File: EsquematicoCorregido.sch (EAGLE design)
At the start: 24 parts, among them IC1 OPA991TIDCKR, IC2 AD8226ARZ-RL, IC3 OPA991TIDCKR, IC4 ESP32-S3-WROOM-1-N16R8, IC5 OPA991TIDCKR, IC6 MAX30102EFD+T, IC7 LP38692MP-3.3_NOPB, IC8 LP38692MP-1.8_NOPB, IC9 REF2033AIDDCT

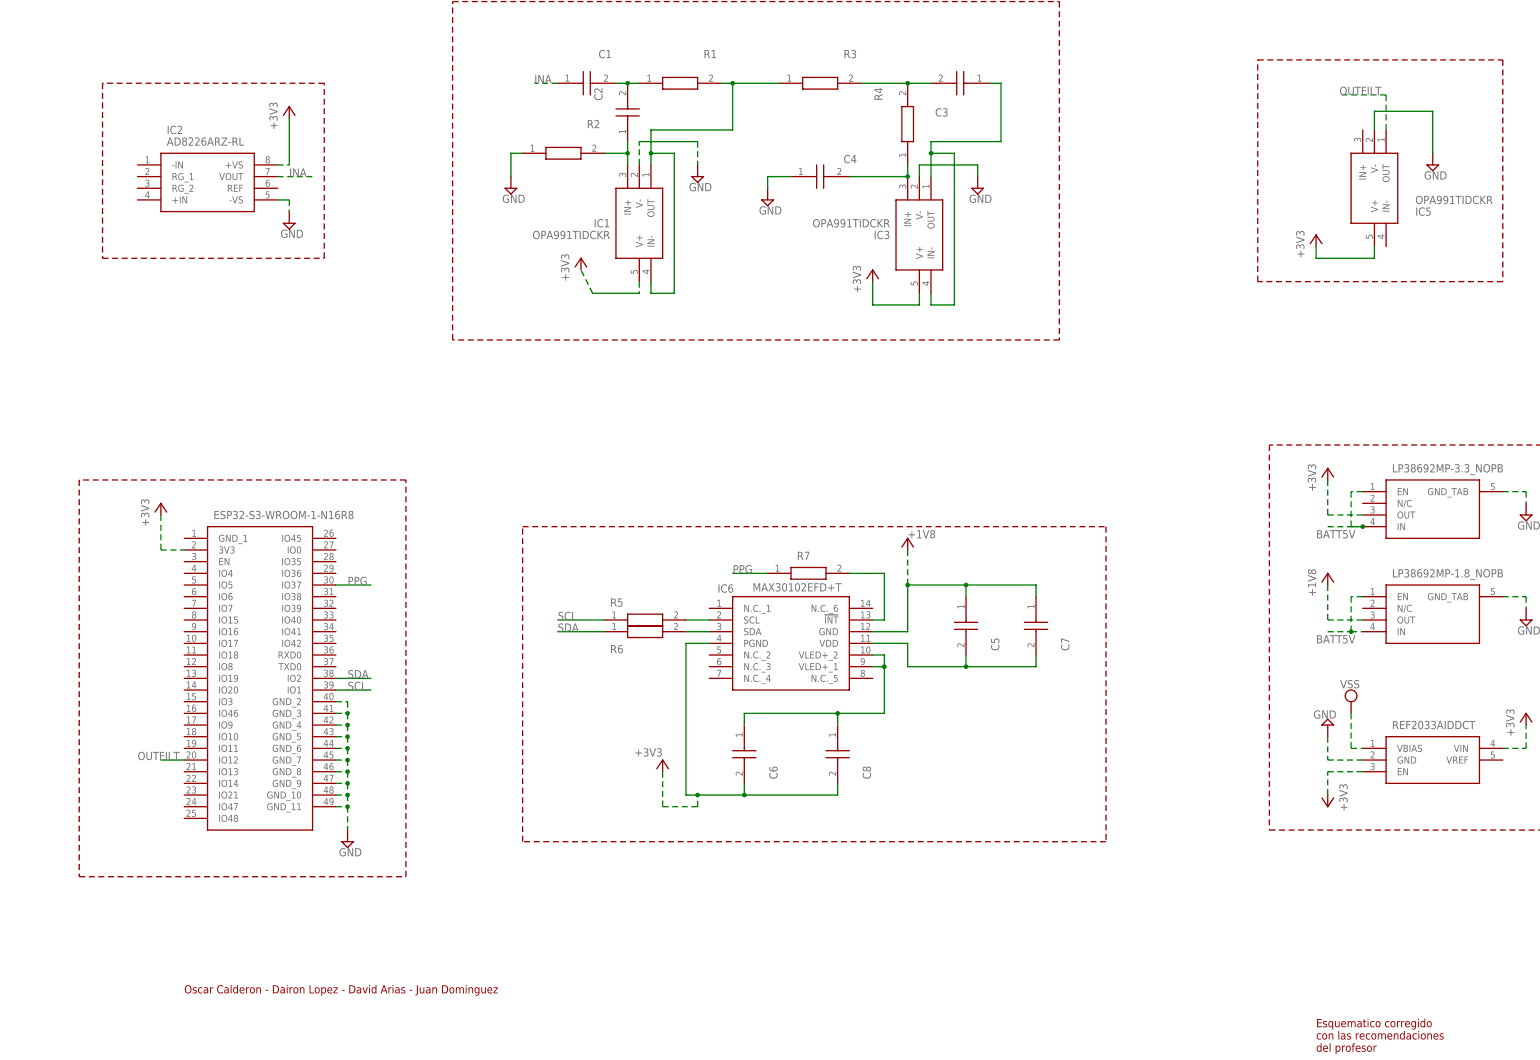
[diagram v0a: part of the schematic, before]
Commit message: Se corrigieron algunos bloques y se anoto lo faltante
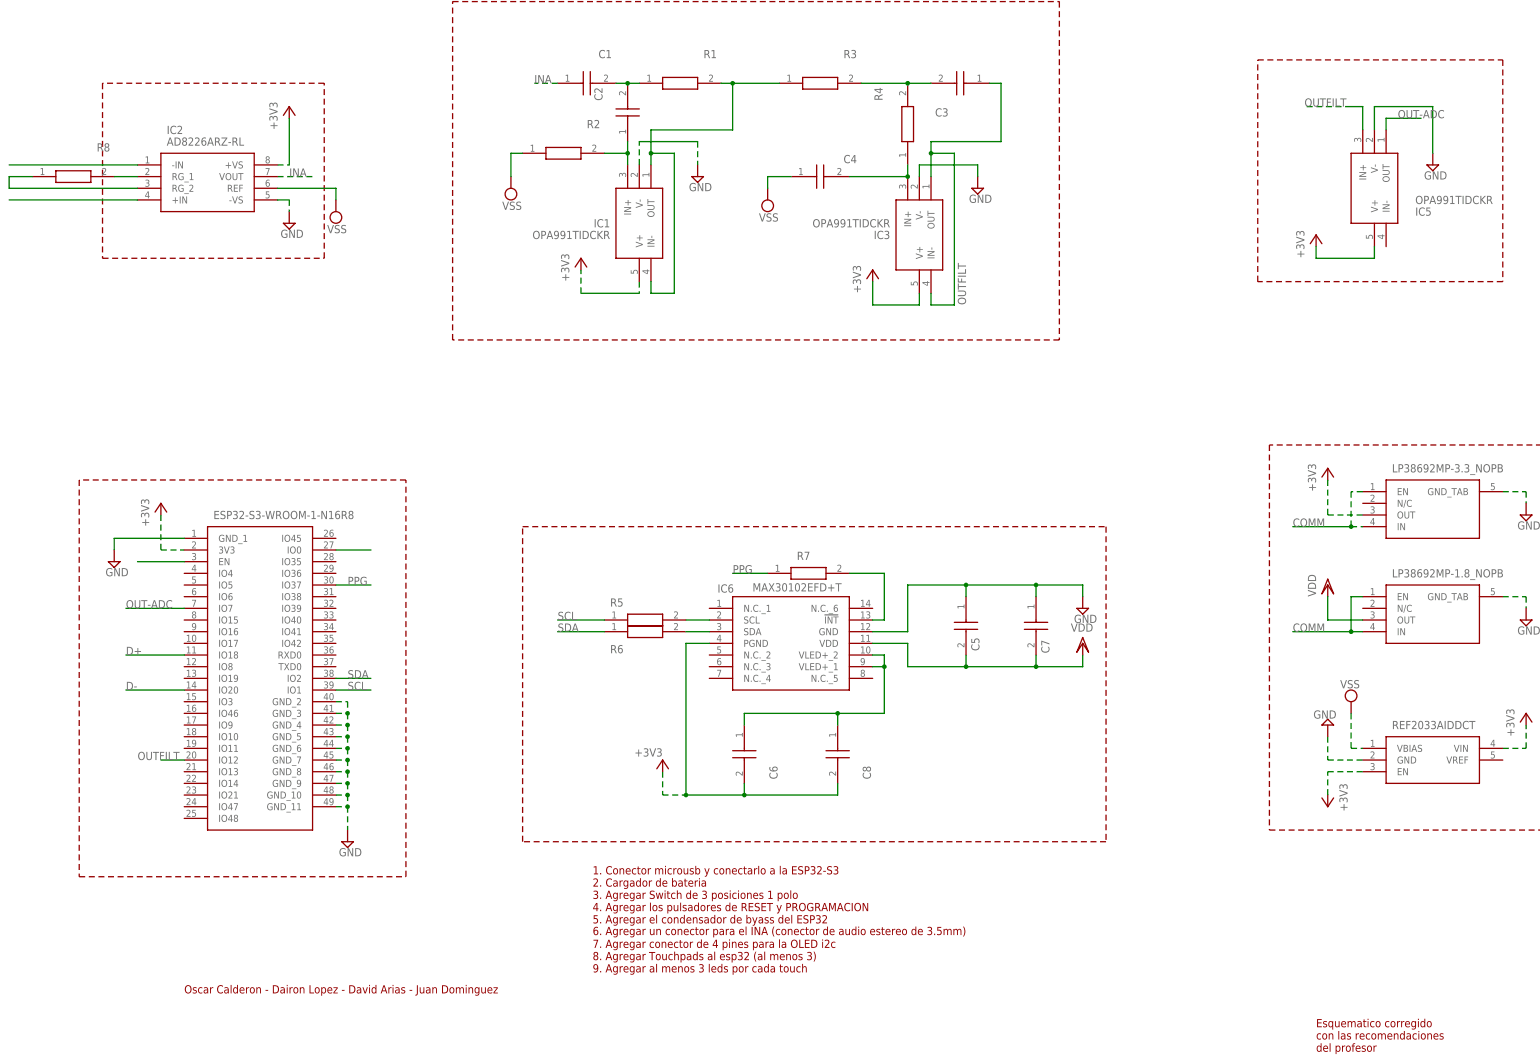
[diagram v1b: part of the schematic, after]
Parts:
- added R8: RN73H1JTTD1043B50, RN73H1JTTD1043B50:RN73H1JTTD1043B50
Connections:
- removed net +1V8: C5.1, C7.1, IC6.GND, IC8.EN, IC8.IN
- removed net BATT5V: IC7.EN, IC7.IN
- removed net N$20: C3.1, IC3.IN-, IC3.OUT
- new net COMM: IC7.EN, IC7.IN, IC8.EN, IC8.IN
- new net D+: IC4.IO18
- new net D-: IC4.IO20
- new net N$10: IC4.EN
- new net N$11: IC2.RG_2, R8.1
- new net N$14: IC2.-IN
- new net N$15: IC2.+IN
- new net N$5: IC4.IO0
- new net OUT-ADC: IC4.IO7, IC5.OUT
- new net VDD: C5.2, C7.2, IC6.VDD, IC8.OUT
- net +3V3: no longer IC8.OUT
- net GND: now also C5.1, C7.1, IC4.GND_1, IC6.GND; no longer C4.1, R2.1
- net N$7: now also IC2.RG_1, R8.2; no longer C5.2, C7.2, IC6.VDD
- net OUTFILT: now also C3.1, IC3.IN-, IC3.OUT, IC5.IN+; no longer IC5.OUT
- net VSS: now also C4.1, IC2.REF, R2.1
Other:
- note added: "1. Conector microusb y conectarlo a la ESP32-S3 2. Cargador de bateria 3. Agregar Switch de 3 posiciones 1 polo 4. Agregar los pulsadores de RESET y PROGRAMACION 5. Agregar el condensador de byass del ESP32"
- note added: "6. Agregar un conector para el INA (conector de audio estereo de 3.5mm)"
- note added: "7. Agregar conector de 4 pines para la OLED i2c 8. Agregar Touchpads al esp32 (al menos 3) 9. Agregar al menos 3 leds por cada touch"

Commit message: ultima actualización, correcion de los puntos
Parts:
- added BAT1: (no value), special:BATTERY
- added C10, C11, C9: GRM155C80G106ME18D, GRM155C80G106ME18D:GRM155C80G106ME18D
- added D1: HLMP6, display-hp:HLMP6
- added IC10: MCP73831T-2ACI_OT, MCP73831T-2ACI_OT:MCP73831T-2ACI_OT
- added J1, J2: USB3131-30-0230-A_REVB, USB3131-30-0230-A_REVB:USB3131-30-0230-A_REVB
- added R10, R11: (no value), resistor-shunt:BVS
- added R2K: ERJ-UP6D2001V, ERJ-UP6D2001V:ERJ-UP6D2001V
- added R9: CRCW0805220RFKTAHP, CRCW0805220RFKTAHP:CRCW0805220RFKTAHP
- added S1, S2: BUTT-2, BUTT-2:BUTT-2
- added U1: DM-OLED096-636, DM-OLED096-636:DM-OLED096-636
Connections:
- removed net N$5: IC4.IO0
- new net 3V3: C11.1, R10.1, R11.1
- new net 5V: C9.2, D1.A, IC10.VDD, J2.VCC
- new net EN: R10.2, S1.1
- new net IO0: IC4.IO0, R11.2, S2.1
- new net N$16: D1.K, R9.2
- new net N$17: IC10.PROG, R2K.2
- new net N$18: IC10.STAT, R9.1
- new net SCL_DSP: IC4.IO9, U1.SCL
- new net SDA_DSP: IC4.IO8, U1.SDA
- net +3V3: now also J1.VCC, U1.VCC_IN
- net D+: now also IC4.IO20, J1.D+; no longer IC4.IO18
- net D-: now also IC4.IO19, J1.D-; no longer IC4.IO20
- net GND: now also C10.1, C11.2, C9.1, IC10.VSS, J1.GND, J1.SHIELD, J2.GND, J2.SHIELD, R2K.1, S1.2, S2.2, U1.GND
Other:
- note added: "1. Conector microusb y conectarlo a la ESP32-S3 (ya) 2. Cargador de bateria(ya) 3. Agregar Switch de 3 posiciones 1 polo 4. Agregar los pulsadores de RESET y PROGRAMACION (ya) 5. Agregar el condensador de byass del ESP32 (ya)"
- note added: "7. Agregar conector de 4 pines para la OLED i2c (ya) 8. Agregar Touchpads al esp32 (al menos 3) 9. Agregar al menos 3 leds por cada touch"
- note removed: "1. Conector microusb y conectarlo a la ESP32-S3 2. Cargador de bateria 3. Agregar Switch de 3 posiciones 1 polo 4. Agregar los pulsadores de RESET y PROGRAMACION 5. Agregar el condensador de byass del ESP32"
- note removed: "7. Agregar conector de 4 pines para la OLED i2c 8. Agregar Touchpads al esp32 (al menos 3) 9. Agregar al menos 3 leds por cada touch"
- moved on the sheet: C1, C2, C3, C4, C5, C6, C7, C8, IC1, IC2, IC3, IC5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

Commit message: Se corrigio el esquematico y packages
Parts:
- removed BAT1: (no value), special:BATTERY
- removed R10, R11: (no value), resistor-shunt:BVS
- removed S1, S2: BUTT-2, BUTT-2:BUTT-2
- added BATT: 1769, 1769:1769
- added C12: (no value), rcl:C-EUC0805
- added POWER: PCM13SMTR, PCM13SMTR:PCM13SMTR
- added R12, R13: (no value), rcl:R-EU_R0805
- added S3, S4: PTS526SK15SMTR2_LFS, PTS526SK15SMTR2_LFS:PTS526SK15SMTR2_LFS
- C1, C3: value QXK2E475KTP -> (none); device QXK2E475KTP:QXK2E475KTP -> rcl:C-EUC0805
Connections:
- new net +5V: C9.2, D1.A, IC10.VDD, POWER.1
- new net BATT+: BATT.2, C10.2, IC10.VBAT, POWER.2
- net 3V3: now also R12.2, R13.2; no longer R10.1, R11.1
- net 5V: no longer C9.2, D1.A, IC10.VDD
- net COMM: now also POWER.3
- net EN: now also R13.1; no longer R10.2, S1.1
- net GND: now also BATT.1, BATT.3, BATT.4; no longer S1.2, S2.2
- net IO0: now also R12.1; no longer R11.2, S2.1

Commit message: ultimas actualizaciones
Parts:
- removed C7: C0805J104K1RACAUTO, C0805J104K1RACAUTO:C0805J104K1RACAUTO
- removed U1: DM-OLED096-636, DM-OLED096-636:DM-OLED096-636
- added SV1: (no value), con-lstb:MA04-1
- C2, C5, C6: value QXK2E475KTP -> (none); device QXK2E475KTP:QXK2E475KTP -> rcl:C-EUC0805
- C4: value C2220X205K1RLCAUTO -> (none); device C2220X205K1RLCAUTO:C2220X205K1RLCAUTO -> rcl:C-EUC0805
- C8: value C0805J104K1RACAUTO -> (none); device C0805J104K1RACAUTO:C0805J104K1RACAUTO -> rcl:C-EUC0805
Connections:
- new net N$21: SV1.1
- net +3V3: now also C4.1, C6.1, SV1.2; no longer C6.2, C8.2, U1.VCC_IN
- net EN: now also S3.NO_1
- net GND: now also C5.2, C8.2, S3.COM_1, S4.COM_1; no longer C5.1, C7.1, U1.GND
- net IO0: now also S4.NO_1
- net N$2: now also C12.2; no longer C2.2
- net N$3: now also C12.1; no longer C2.1
- net N$4: now also C2.2; no longer C4.2
- net N$9: now also C4.2, C6.2; no longer C6.1, C8.1
- net SCL_DSP: now also SV1.4; no longer U1.SCL
- net SDA_DSP: now also SV1.3; no longer U1.SDA
- net VDD: now also C5.1, C8.1; no longer C5.2, C7.2
- net VSS: now also C2.1; no longer C4.1
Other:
- note added: "1. Conector microusb y conectarlo a la ESP32-S3 (ya) 2. Cargador de bateria(ya) 3. Agregar Switch de 3 posiciones 1 polo (ya) 4. Agregar los pulsadores de RESET y PROGRAMACION (ya) 5. Agregar el condensador de byass del ESP32 (ya)"
- note removed: "1. Conector microusb y conectarlo a la ESP32-S3 (ya) 2. Cargador de bateria(ya) 3. Agregar Switch de 3 posiciones 1 polo 4. Agregar los pulsadores de RESET y PROGRAMACION (ya) 5. Agregar el condensador de byass del ESP32 (ya)"
- moved on the sheet: C11, C12, POWER, R12, R13, S3, S4

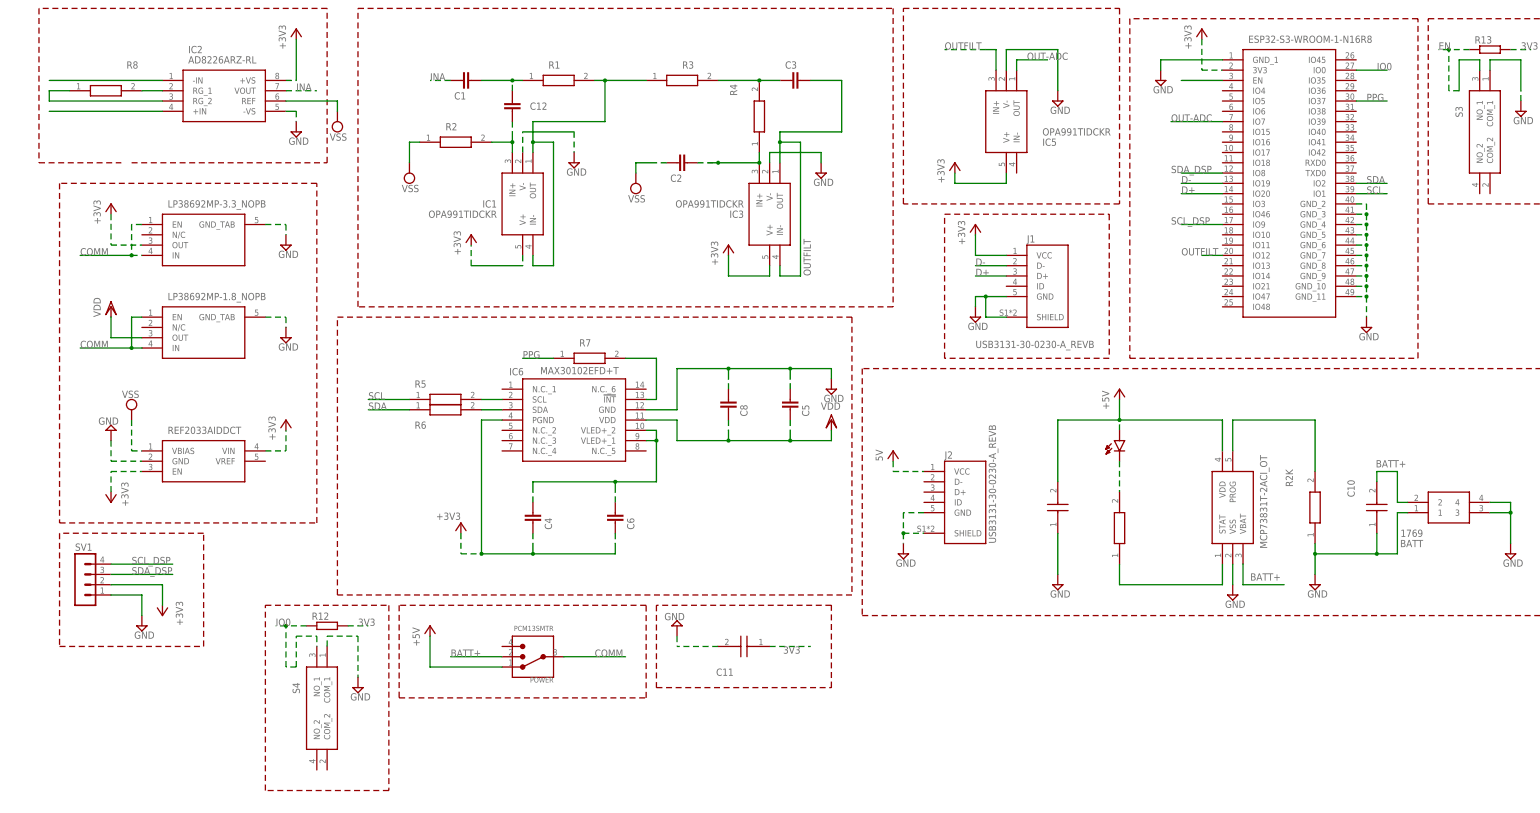
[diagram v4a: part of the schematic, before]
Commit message: fix: PCB and schematic errors fixed
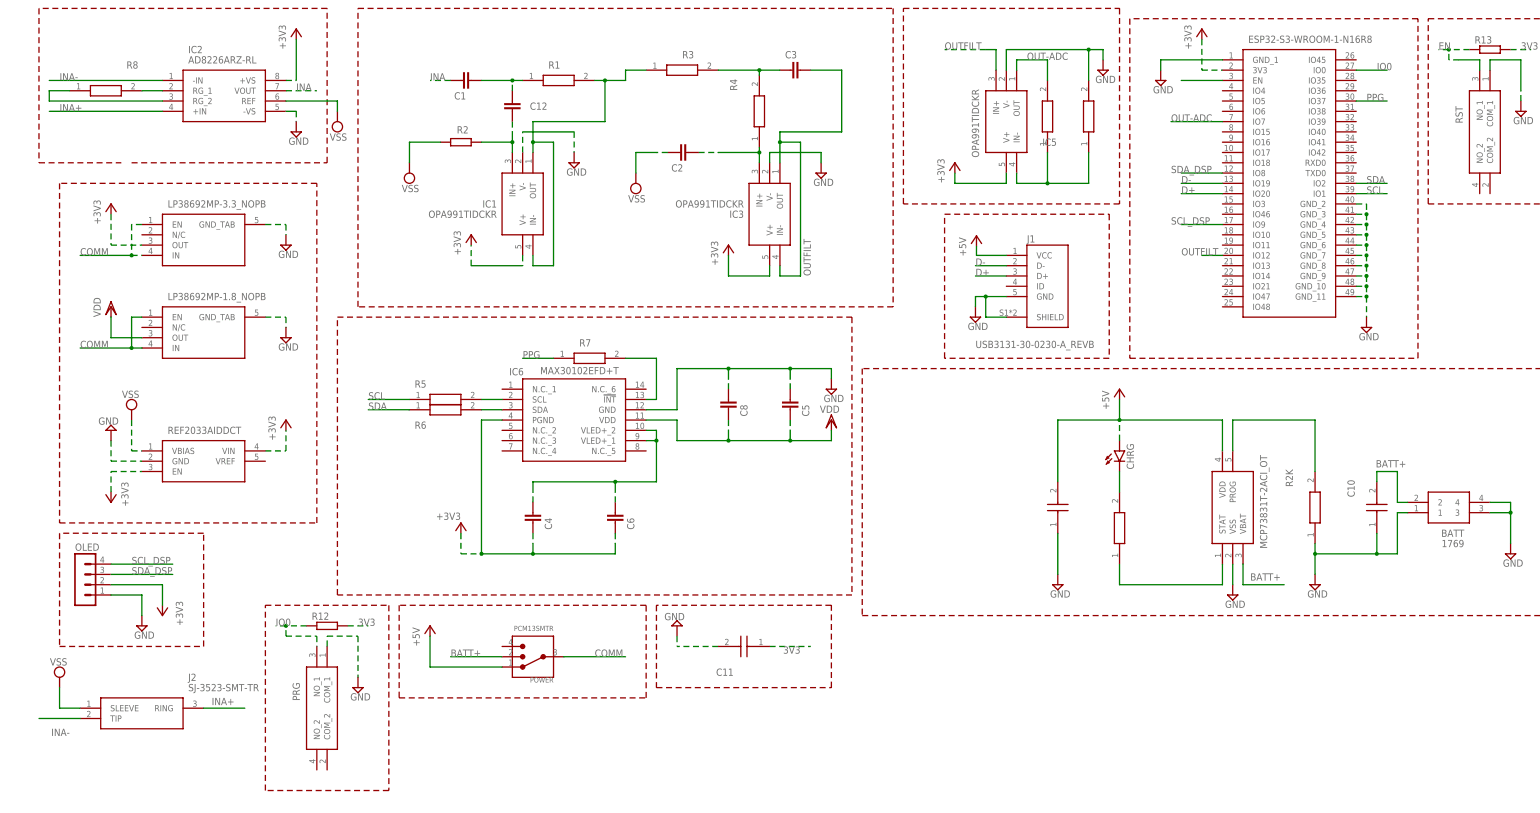
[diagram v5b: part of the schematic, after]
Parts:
- removed D1: HLMP6, display-hp:HLMP6
- added CHRG: (no value), led:LEDCHIP-LED0805
- added R10, R11: CRCW0805220RFKTAHP, CRCW0805220RFKTAHP:CRCW0805220RFKTAHP
- J2: value USB3131-30-0230-A_REVB -> SJ-3523-SMT-TR; device USB3131-30-0230-A_REVB:USB3131-30-0230-A_REVB -> SJ-3523-SMT-TR:SJ-3523-SMT-TR
- R2: value RN73H1JTTD1043B50 -> (none); device RN73H1JTTD1043B50:RN73H1JTTD1043B50 -> rcl:R-EU_R0805
- renumbered S3 to RST, S4 to PRG, SV1 to OLED
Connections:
- removed net 5V: J2.VCC
- removed net N$15: IC2.+IN
- removed net N$16: D1.K, R9.2
- new net INA+: IC2.+IN, J2.RING
- new net INA-: IC2.-IN, J2.TIP
- new net N$5: IC5.IN-, R10.1, R11.1
- net +3V3: no longer J1.VCC
- net +5V: now also CHRG.A, J1.VCC; no longer D1.A
- net GND: now also R11.2; no longer J2.GND, J2.SHIELD
- net N$14: now also CHRG.C, R9.2; no longer IC2.-IN
- net OUT-ADC: now also R10.2
- net VSS: now also J2.SLEEVE
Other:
- moved on the sheet: C2, C3, R3, R4

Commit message: Avance PCB
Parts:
- removed J1: USB3131-30-0230-A_REVB, USB3131-30-0230-A_REVB:USB3131-30-0230-A_REVB
- removed R2K: ERJ-UP6D2001V, ERJ-UP6D2001V:ERJ-UP6D2001V
- added J3: USB4216-03-A, USB4216-03-A:USB4216-03-A
- added R14, R15, R16: (no value), rcl:R-EU_R0805
- C10, C11, C9: value GRM155C80G106ME18D -> (none); device GRM155C80G106ME18D:GRM155C80G106ME18D -> rcl:C-EUC0805
- R1: value RN73H1ETTP4812D25 -> (none); device RN73H1ETTP4812D25:RN73H1ETTP4812D25 -> rcl:R-EU_R0805
- R9: value CRCW0805220RFKTAHP -> (none); device CRCW0805220RFKTAHP:CRCW0805220RFKTAHP -> rcl:R-EU_R0805
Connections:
- removed net N$10: IC4.EN
- new net N$16: J3.CC1, R15.1
- new net N$19: J3.CC2, R16.2
- net +3V3: now also R12.2, R13.2
- net +5V: now also C9.1, J3.VBUS_1, J3.VBUS_2; no longer C9.2, J1.VCC
- net 3V3: now also C11.2; no longer C11.1, R12.2, R13.2
- net BATT+: now also C10.1; no longer C10.2
- net D+: now also J3.DP1, J3.DP2; no longer J1.D+
- net D-: now also J3.DN1, J3.DN2; no longer J1.D-
- net EN: now also IC4.EN
- net GND: now also C10.2, C11.1, C9.2, J3.GND_1, J3.GND_2, J3.GND_3, J3.GND_4, J3.GND_5, J3.GND_6, R14.1, R15.2, R16.1; no longer C10.1, C11.2, C9.1, J1.GND, J1.SHIELD, R2K.1
- net N$17: now also R14.2; no longer R2K.2
